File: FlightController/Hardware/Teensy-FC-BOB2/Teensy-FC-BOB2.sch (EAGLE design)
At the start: 37 parts, among them U1 MPU-9250, U3 BMP180;314030004

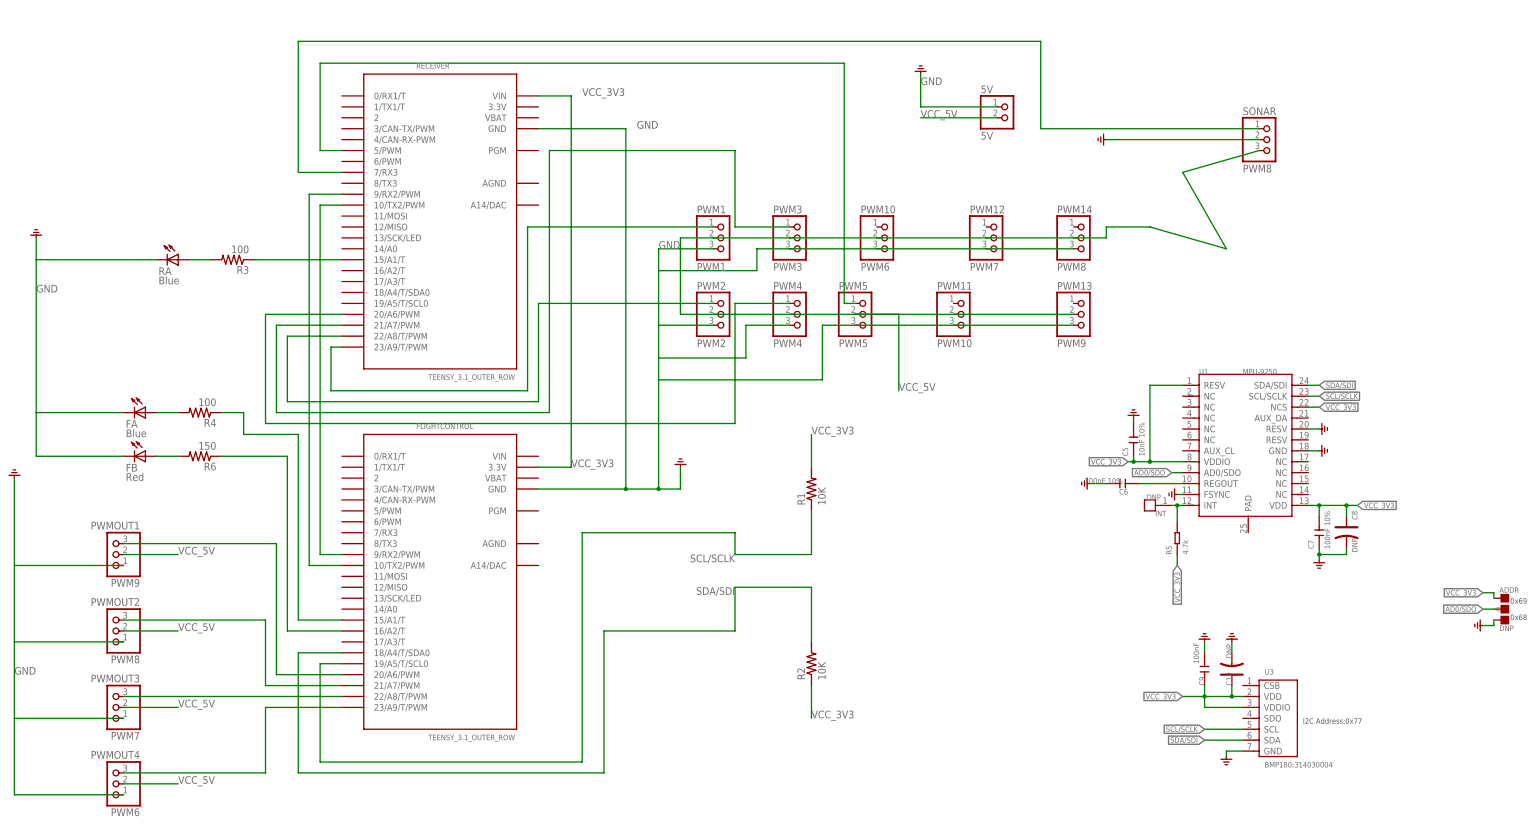
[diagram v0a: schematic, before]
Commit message: autoroutes the pub
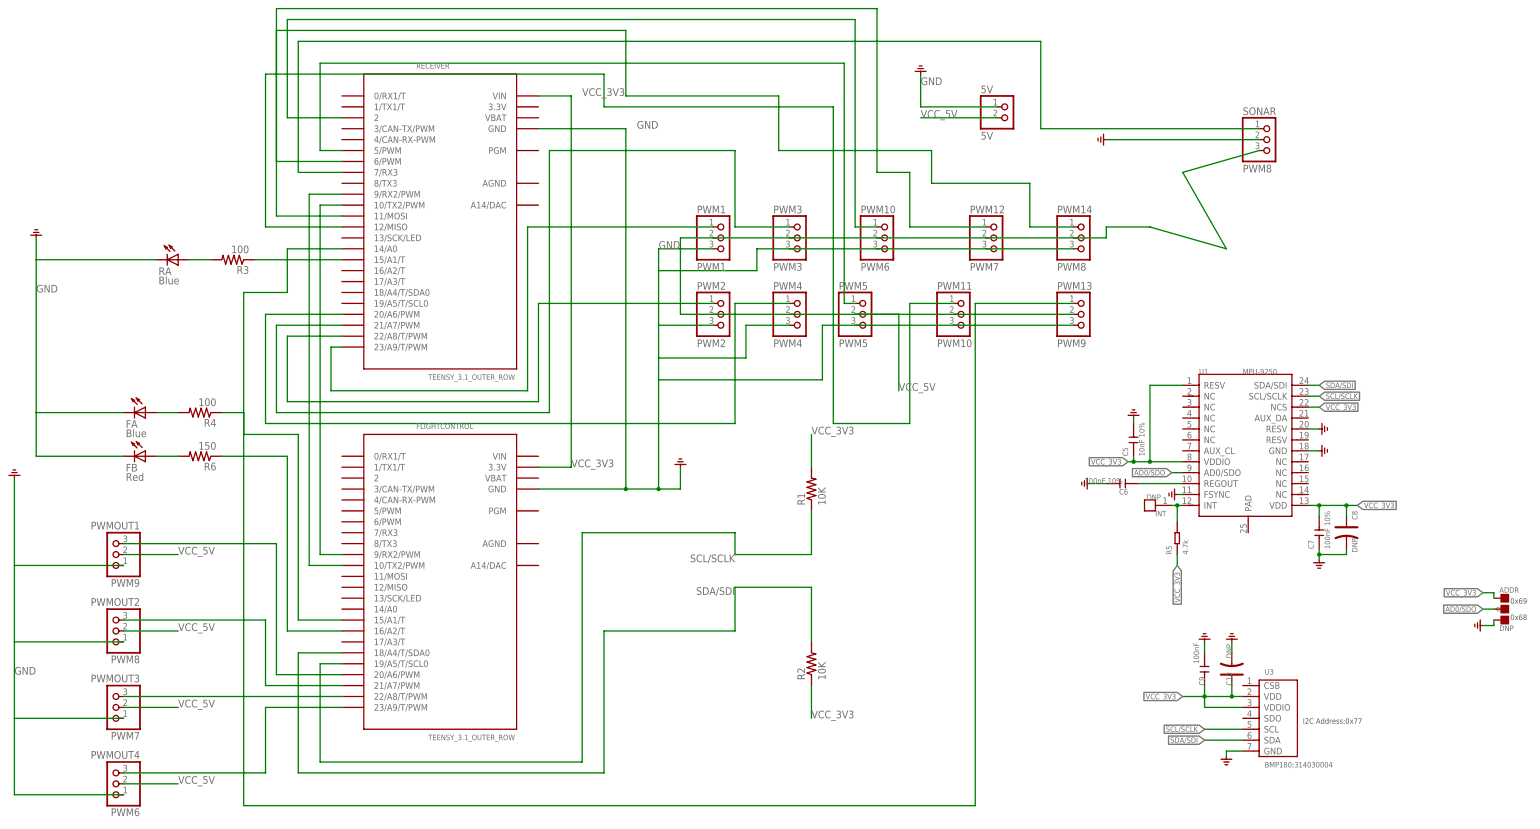
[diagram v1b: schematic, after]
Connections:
- new net N$20: PWM10.1, RECEIVER.2
- new net N$23: PWM12.1, RECEIVER.6/PWM
- new net N$24: PWM14.1, RECEIVER.11/MOSI
- new net N$25: PWM11.1, RECEIVER.12/MISO
- new net N$26: PWM13.1, RECEIVER.14/A0
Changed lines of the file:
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@@
 <?xml version="1.0" encoding="utf-8"?>
 <!DOCTYPE eagle SYSTEM "eagle.dtd">
-<eagle version="7.7.0">
+<eagle version="8.0.0">
 <drawing>
 <settings>
@@
 </segment>
 </net>
+<net name="N$20" class="0">
+<segment>
+<pinref part="PWM10" gate="A" pin="1"/>
+<wire x1="45.72" y1="129.54" x2="40.64" y2="129.54" width="0.1524" layer="91"/>
+<wire x1="40.64" y1="129.54" x2="40.64" y2="177.8" width="0.1524" layer="91"/>
+<wire x1="40.64" y1="177.8" x2="-91.44" y2="177.8" width="0.1524" layer="91"/>
+<wire x1="-91.44" y1="177.8" x2="-91.44" y2="154.94" width="0.1524" layer="91"/>
+<pinref part="RECEIVER" gate="G$1" pin="2"/>
+<wire x1="-91.44" y1="154.94" x2="-78.74" y2="154.94" width="0.1524" layer="91"/>
+</segment>
+</net>
+<net name="N$23" class="0">
+<segment>
+<pinref part="PWM12" gate="A" pin="1"/>
+<wire x1="71.12" y1="129.54" x2="53.34" y2="129.54" width="0.1524" layer="91"/>
+<wire x1="53.34" y1="129.54" x2="53.34" y2="142.24" width="0.1524" layer="91"/>
+<wire x1="53.34" y1="142.24" x2="45.72" y2="142.24" width="0.1524" layer="91"/>
+<wire x1="45.72" y1="142.24" x2="45.72" y2="180.34" width="0.1524" layer="91"/>
+<wire x1="45.72" y1="180.34" x2="-93.98" y2="180.34" width="0.1524" layer="91"/>
+<wire x1="-93.98" y1="180.34" x2="-93.98" y2="144.78" width="0.1524" layer="91"/>
+<pinref part="RECEIVER" gate="G$1" pin="6/PWM"/>
+<wire x1="-93.98" y1="144.78" x2="-78.74" y2="144.78" width="0.1524" layer="91"/>
+</segment>
+</net>
+<net name="N$24" class="0">
+<segment>
+<pinref part="PWM14" gate="A" pin="1"/>
+<wire x1="91.44" y1="129.54" x2="81.28" y2="129.54" width="0.1524" layer="91"/>
+<wire x1="81.28" y1="129.54" x2="81.28" y2="139.7" width="0.1524" layer="91"/>
+<wire x1="81.28" y1="139.7" x2="58.42" y2="139.7" width="0.1524" layer="91"/>
+<wire x1="58.42" y1="139.7" x2="58.42" y2="147.32" width="0.1524" layer="91"/>
+<wire x1="58.42" y1="147.32" x2="22.86" y2="147.32" width="0.1524" layer="91"/>
+<wire x1="22.86" y1="147.32" x2="22.86" y2="160.02" width="0.1524" layer="91"/>
+<wire x1="22.86" y1="160.02" x2="-12.7" y2="160.02" width="0.1524" layer="91"/>
+<wire x1="-12.7" y1="160.02" x2="-12.7" y2="175.26" width="0.1524" layer="91"/>
+<wire x1="-12.7" y1="175.26" x2="-93.98" y2="175.26" width="0.1524" layer="91"/>
+<wire x1="-93.98" y1="175.26" x2="-93.98" y2="132.08" width="0.1524" layer="91"/>
+<pinref part="RECEIVER" gate="G$1" pin="11/MOSI"/>
+<wire x1="-93.98" y1="132.08" x2="-78.74" y2="132.08" width="0.1524" layer="91"/>
+</segment>
+</net>
+<net name="N$25" class="0">
+<segment>
+<pinref part="PWM11" gate="A" pin="1"/>
+<wire x1="63.5" y1="111.76" x2="53.34" y2="111.76" width="0.1524" layer="91"/>
+<wire x1="53.34" y1="111.76" x2="53.34" y2="83.82" width="0.1524" layer="91"/>
+<wire x1="53.34" y1="83.82" x2="35.56" y2="83.82" width="0.1524" layer="91"/>
+<wire x1="35.56" y1="83.82" x2="35.56" y2="157.48" width="0.1524" layer="91"/>
+<wire x1="35.56" y1="157.48" x2="-17.78" y2="157.48" width="0.1524" layer="91"/>
+<wire x1="-17.78" y1="157.48" x2="-17.78" y2="165.1" width="0.1524" layer="91"/>
+<wire x1="-17.78" y1="165.1" x2="-96.52" y2="165.1" width="0.1524" layer="91"/>
+<wire x1="-96.52" y1="165.1" x2="-96.52" y2="129.54" width="0.1524" layer="91"/>
+<pinref part="RECEIVER" gate="G$1" pin="12/MISO"/>
+<wire x1="-96.52" y1="129.54" x2="-78.74" y2="129.54" width="0.1524" layer="91"/>
+</segment>
+</net>
+<net name="N$26" class="0">
+<segment>
+<pinref part="PWM13" gate="A" pin="1"/>
+<wire x1="91.44" y1="111.76" x2="68.58" y2="111.76" width="0.1524" layer="91"/>
+<wire x1="68.58" y1="111.76" x2="68.58" y2="-5.08" width="0.1524" layer="91"/>
+<wire x1="68.58" y1="-5.08" x2="-101.6" y2="-5.08" width="0.1524" layer="91"/>
+<wire x1="-101.6" y1="-5.08" x2="-101.6" y2="114.3" width="0.1524" layer="91"/>
+<wire x1="-101.6" y1="114.3" x2="-91.44" y2="114.3" width="0.1524" layer="91"/>
+<wire x1="-91.44" y1="114.3" x2="-91.44" y2="124.46" width="0.1524" layer="91"/>
+<pinref part="RECEIVER" gate="G$1" pin="14/A0"/>
+<wire x1="-91.44" y1="124.46" x2="-78.74" y2="124.46" width="0.1524" layer="91"/>
+</segment>
+</net>
